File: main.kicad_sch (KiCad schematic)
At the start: 15 parts, among them J1 Conn_02x16_Row_Letter_First

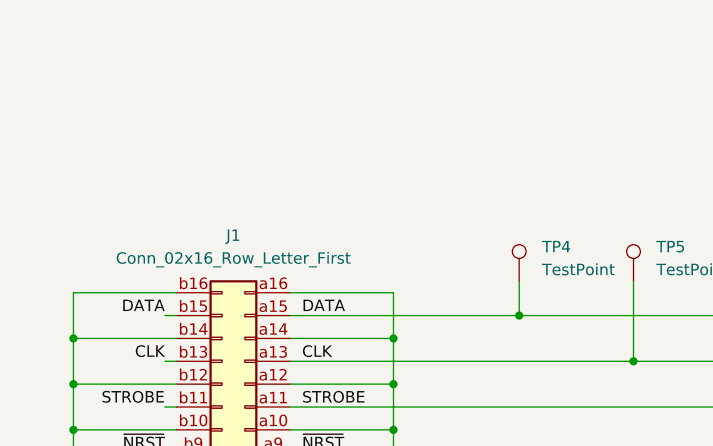
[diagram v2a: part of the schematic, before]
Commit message: update after component procurement problems
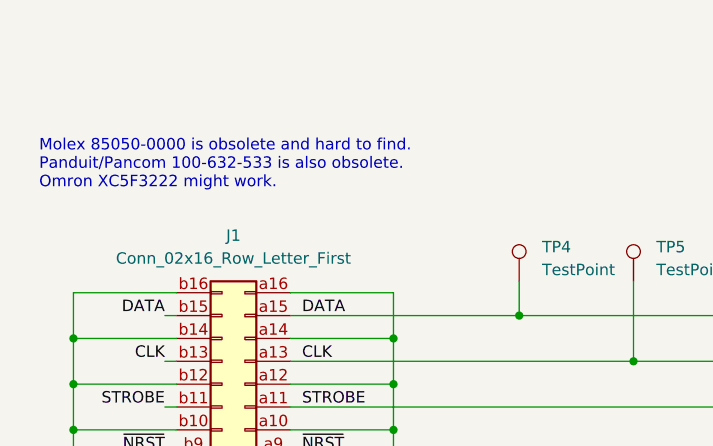
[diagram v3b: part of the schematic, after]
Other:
- note added: "Molex 85050-0000 is obsolete and hard to find. Panduit/Pancom 100-632-533 is also obsolete. Omron XC5F3222 might work."
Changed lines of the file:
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@@
+    (effects (font (size 1.27 1.27)) (justify left bottom))
+  )
+  (text "Molex 85050-0000 is obsolete and hard to find.\nPanduit/Pancom 100-632-533 is also obsolete.\nOmron XC5F3222 might work."
+    (at 24.13 43.18 0)
     (effects (font (size 1.27 1.27)) (justify left bottom))
   )

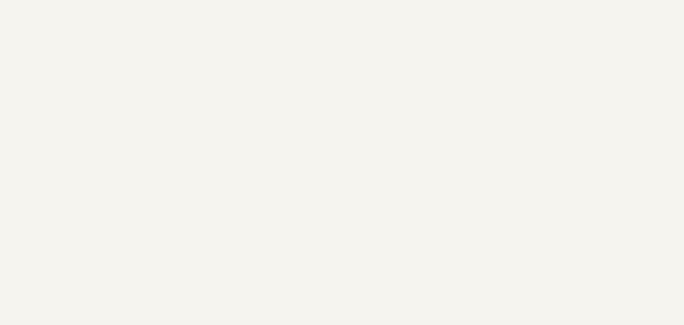
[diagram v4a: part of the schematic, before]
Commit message: Revised barriers, modified the PCB to comply with related standards, rerouted traces.
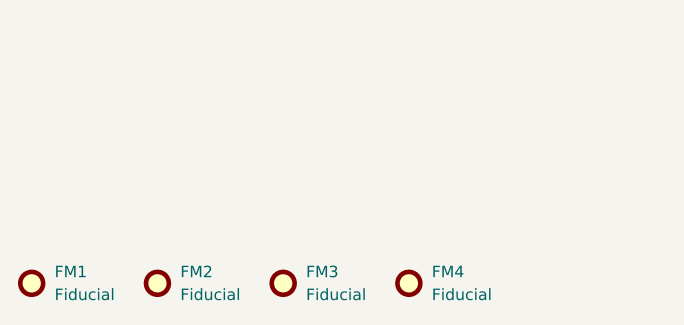
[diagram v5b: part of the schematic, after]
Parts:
- added FM1, FM2, FM3, FM4: Fiducial, Fiducial:Fiducial_1mm_Mask2mm, symbol Mechanical:Fiducial
- SYM1: footprint Symbol:Symbol_Highvoltage_Type2_CopperTop_Small -> Symbol:Symbol_HighVoltage_Triangle_17x15mm_Copper
